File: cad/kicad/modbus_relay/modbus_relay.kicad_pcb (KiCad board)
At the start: 4 copper layers, 75 x 107 mm, 145 parts, among them J10 Conn_02x03_Odd_Even, J11 Screw_Terminal_01x02, J2 Screw_Terminal_01x03, J4 Screw_Terminal_01x02, J5 Screw_Terminal_01x03, J6 Screw_Terminal_01x03, J7 Screw_Terminal_01x03, J8 Screw_Terminal_01x03, J9 Screw_Terminal_01x02, K1 Relay_SPDT, Q1 BSS138, Q2 BSS138, Q3 BSS138, Q4 BSS138, Q6 AO3401A, SW1 SW_Push, U1 LT1785AxS8, U2 ATtiny3227-M, U3 LMR33630ADDA, U4 AMC3330

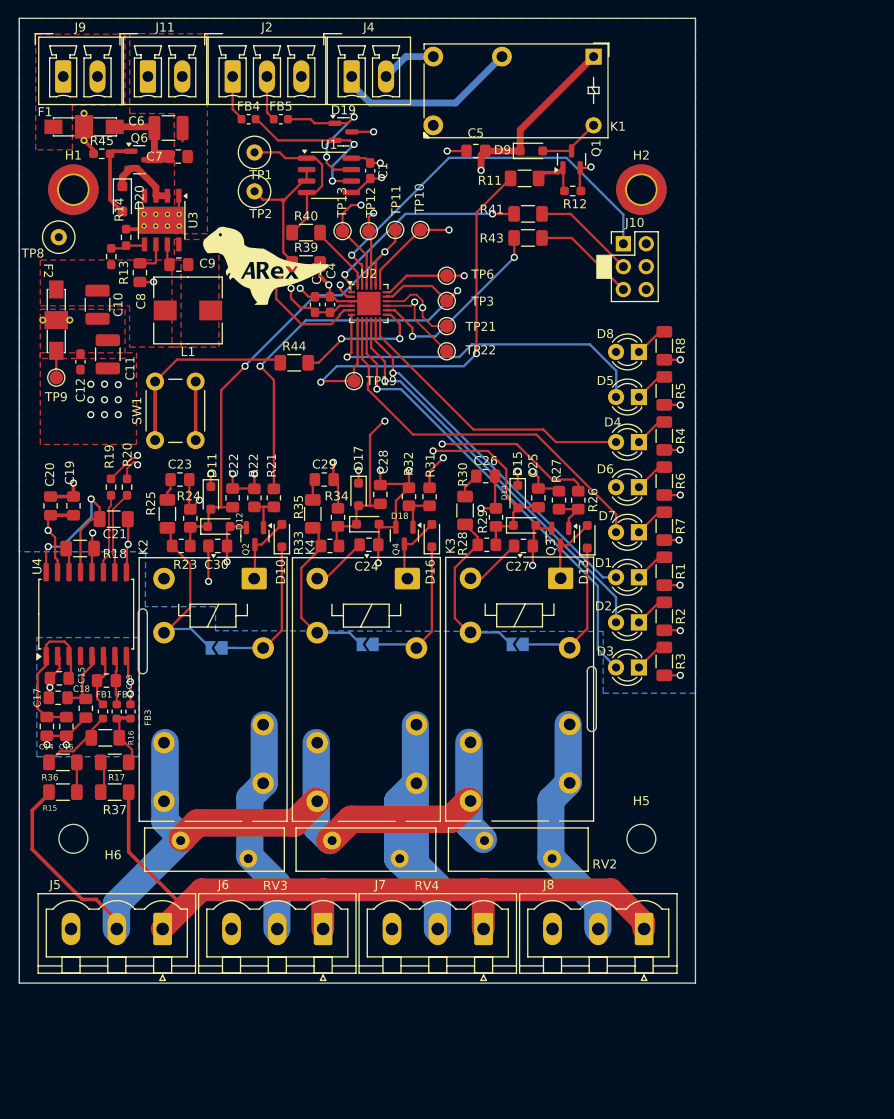
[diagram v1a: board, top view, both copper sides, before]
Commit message: Double sided version
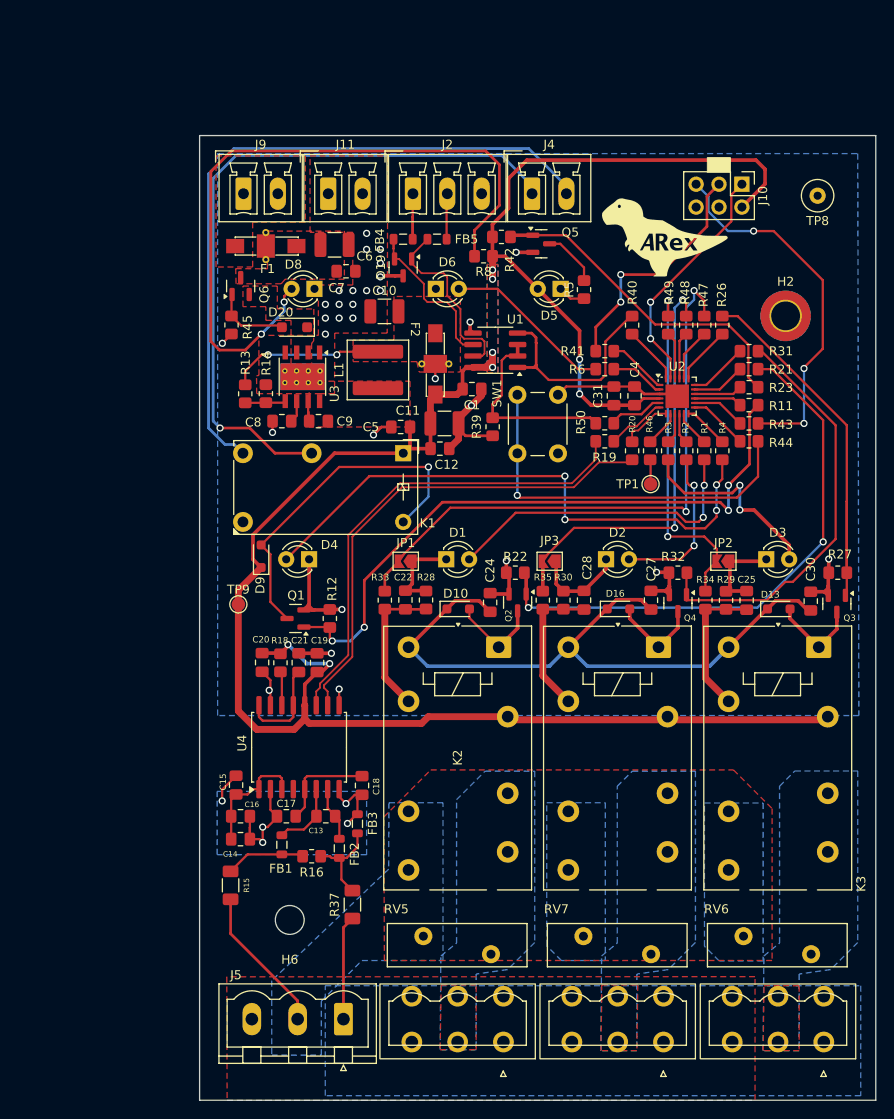
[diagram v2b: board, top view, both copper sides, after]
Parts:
- removed C23, C26, C29: 100n, Capacitor_SMD:C_0805_2012Metric_Pad1.18x1.45mm_HandSolder
- removed D11, D12, D14, D15, D17, D18: BAS16, Diode_SMD:D_SOD-323_HandSoldering
- removed D7: G, LED_THT:LED_D3.0mm
- removed H1: MountingHole_Pad, MountingHole:MountingHole_3.2mm_M3_DIN965_Pad_TopBottom
- removed H5: MountingHole, MountingHole:MountingHole_3.2mm_M3
- removed J6: Screw_Terminal_01x03, Connector_Phoenix_MSTB:PhoenixContact_MSTBVA_2,5_3-G-5,08_1x03_P5.08mm_Vertical
- removed R17, R36: 20K, Resistor_SMD:R_1206_3216Metric_Pad1.30x1.75mm_HandSolder
- removed R24: 1k, Resistor_SMD:R_0805_2012Metric_Pad1.20x1.40mm_HandSolder
- removed R25: 100, Resistor_SMD:R_1206_3216Metric_Pad1.30x1.75mm_HandSolder
- removed R7: 680, Resistor_SMD:R_1206_3216Metric_Pad1.30x1.75mm_HandSolder
- removed RV2, RV3, RV4: 471K, adarwoo:MOV471
- removed TP10, TP11, TP12, TP13, TP19, TP21, TP22, TP3, TP6: TestPoint_Small, TestPoint:TestPoint_Pad_D1.5mm
- removed TP2: TestPoint, TestPoint:TestPoint_Loop_D3.50mm_Drill0.9mm_Beaded
- added J12: 1785955, Phenix contact:CONN_1943548, F.Cu at (156.4, 141.0)
- added Q5: BSS138, Package_TO_SOT_SMD:SOT-23, F.Cu at (147.9, 55.0)
- added R42: 10k, Resistor_SMD:R_0805_2012Metric_Pad1.20x1.40mm_HandSolder, F.Cu at (143.5, 54.2)
- added R46: 332, Resistor_SMD:R_0805_2012Metric_Pad1.20x1.40mm_HandSolder, F.Cu at (160.0, 78.0)
- added R47: 332, Resistor_SMD:R_0805_2012Metric_Pad1.20x1.40mm_HandSolder, F.Cu at (166.0, 64.0)
- added R48: 332, Resistor_SMD:R_0805_2012Metric_Pad1.20x1.40mm_HandSolder, F.Cu at (164.0, 64.0)
- added R49: 332, Resistor_SMD:R_0805_2012Metric_Pad1.20x1.40mm_HandSolder, F.Cu at (162.0, 64.0)
- added R50: 332, Resistor_SMD:R_0805_2012Metric_Pad1.20x1.40mm_HandSolder, F.Cu at (154.9, 74.9)
- added RV5: 471K, adarwoo:MOV471, F.Cu at (138.6, 133.0)
- added RV6: 471K, adarwoo:MOV471, F.Cu at (174.1, 133.0)
- added RV7: 471K, adarwoo:MOV471, F.Cu at (156.4, 133.0)
- C1, C12, C31, C4: footprint Capacitor_SMD:C_0603_1608Metric_Pad1.08x0.95mm_HandSolder -> Capacitor_SMD:C_0805_2012Metric_Pad1.18x1.45mm_HandSolder
- C21: footprint Capacitor_SMD:C_1206_3216Metric_Pad1.33x1.80mm_HandSolder -> Capacitor_SMD:C_0805_2012Metric_Pad1.18x1.45mm_HandSolder
- D20: value BZT52B51 -> BZT52B12
- FB1, FB2, FB3, FB4, FB5: footprint Inductor_SMD:L_0603_1608Metric -> Inductor_SMD:L_0805_2012Metric
- J7, J8: value Screw_Terminal_01x03 -> 1785955; footprint Connector_Phoenix_MSTB:PhoenixContact_MSTBVA_2,5_3-G-5,08_1x03_P5.08mm_Vertical -> Phenix contact:CONN_1943548
- JP1, JP2, JP3: moved to F.Cu
- L1: value 15uH -> 10uH; footprint Inductor_SMD:L_Wuerth_HCM-7070 -> Inductor_SMD:L_Bourns_SRP6060FA
- R1, R11, R16, R18, R2, R3, R39, R4, R40, R41, R43, R44, R5, R6, R8: footprint Resistor_SMD:R_1206_3216Metric_Pad1.30x1.75mm_HandSolder -> Resistor_SMD:R_0805_2012Metric_Pad1.20x1.40mm_HandSolder
- R12, R13, R14, R19, R20: footprint Resistor_SMD:R_0603_1608Metric_Pad0.98x0.95mm_HandSolder -> Resistor_SMD:R_0805_2012Metric_Pad1.20x1.40mm_HandSolder
- R23: value 3k83 -> 22
- R28, R33: value 3k83 -> 332
- R29, R34: value 1k -> 332
- R30, R35: value 100 -> 332; footprint Resistor_SMD:R_1206_3216Metric_Pad1.30x1.75mm_HandSolder -> Resistor_SMD:R_0805_2012Metric_Pad1.20x1.40mm_HandSolder
- R45: value 22 -> 10K; footprint Resistor_SMD:R_0603_1608Metric_Pad0.98x0.95mm_HandSolder -> Resistor_SMD:R_0805_2012Metric_Pad1.20x1.40mm_HandSolder
- TP1: value TestPoint -> TestPoint_Probe; footprint TestPoint:TestPoint_Loop_D3.50mm_Drill0.9mm_Beaded -> TestPoint:TestPoint_Pad_D1.5mm
- moved TP8 84.3 mm to (178.5, 49.7)
- moved C30 66.1 mm to (177.8, 94.6), turned to 90 degrees
- moved R23 65.4 mm to (170.9, 70.9)
- moved Q1 59.4 mm to (120.6, 96.6), turned to 180 degrees
- moved TP1 57.3 mm to (160.0, 81.7)
- moved R20 56.2 mm to (158.0, 78.0)
- moved R19 55.0 mm to (154.9, 76.9), turned to 0 degrees
- moved R21 54.6 mm to (170.9, 68.9), turned to 0 degrees
- moved R12 54.5 mm to (124.4, 96.6), turned to 90 degrees
- moved D9 54.0 mm to (116.8, 89.7), turned to 90 degrees
- moved R44 51.2 mm to (170.9, 76.9), turned to 180 degrees
- moved K1 48.8 mm to (132.6, 78.2)
- moved G*** 44.4 mm to (161.6, 54.3)
- moved F2 42.3 mm to (136.1, 68.3)
- moved R34 41.8 mm to (166.1, 94.5), turned to -90 degrees
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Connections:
- net Net-(D19-A1) renamed /FILT+
- net Net-(D19-A2) renamed /FILT-
- C22 pad 1: RELAY_CHECK_1 -> Net-(C22-Pad1)
- C24 pad 1: +24V -> V_IN
- C25 pad 1: RELAY_CHECK_3 -> Net-(C25-Pad1)
- C27 pad 1: +24V -> V_IN
- C28 pad 1: RELAY_CHECK_2 -> Net-(C28-Pad1)
- C30 pad 1: +24V -> V_IN
- D1 pad 1: Net-(D1-K) -> GND
- D1 pad 2: LED_RELAY_1 -> Net-(D1-A)
- D10 pad 1: +24V -> V_IN
- D13 pad 1: +24V -> V_IN
- D16 pad 1: +24V -> V_IN
- D2 pad 1: Net-(D2-K) -> GND
- D2 pad 2: LED_RELAY_2 -> Net-(D2-A)
- D3 pad 1: Net-(D3-K) -> GND
- D3 pad 2: LED_RELAY_3 -> Net-(D3-A)
- D4 pad 1: Net-(D4-K) -> GND
- D4 pad 2: LED_MAINS -> Net-(D4-A)
- D5 pad 2: LED_FAULT -> VCC
- D6 pad 1: Net-(D6-K) -> GND
- D6 pad 2: LED_RX -> Net-(D6-A)
- D8 pad 1: Net-(D8-K) -> GND
- D8 pad 2: VCC -> Net-(D8-A)
- J7 pad 2: RELAY_OUT_2 -> MAINS_N
- J7 pad 3: Earth -> RELAY_OUT_1
- J8 pad 2: RELAY_OUT_3 -> MAINS_N
- J8 pad 3: Earth -> RELAY_OUT_3
- JP1 pad 1: +24V -> GND
- JP1 pad 2: Net-(JP1-B) -> RELAY_CHECK_1
- JP2 pad 1: +24V -> GND
- JP2 pad 2: Net-(JP2-B) -> RELAY_CHECK_3
- JP3 pad 1: +24V -> GND
- JP3 pad 2: Net-(JP3-B) -> RELAY_CHECK_2
- K2 pad 11: Net-(JP1-B) -> Net-(C22-Pad1)
- K2 pad 12: +24V -> VCC
- K2 pad A1: +24V -> V_IN
- K3 pad 11: Net-(JP2-B) -> Net-(C25-Pad1)
- K3 pad 12: +24V -> VCC
- K3 pad A1: +24V -> V_IN
- K4 pad 11: Net-(JP3-B) -> Net-(C28-Pad1)
- K4 pad 12: +24V -> VCC
- K4 pad A1: +24V -> V_IN
- R1 pad 1: Net-(D1-K) -> LED_RELAY_1
- R1 pad 2: GND -> Net-(D1-A)
- R11 pad 1: ES_CMD -> ~{ESTOP}
- R15 pad 2: Net-(R15-Pad2) -> Net-(FB1-Pad1)
- R2 pad 1: Net-(D2-K) -> LED_RELAY_2
- R2 pad 2: GND -> Net-(D2-A)
- R23 pad 1: Net-(JP1-B) -> ~{LED_FAULT}
- R23 pad 2: RELAY_CHECK_1 -> Net-(Q5-G)
- R28 pad 1: Net-(JP2-B) -> Net-(C22-Pad1)
- R28 pad 2: RELAY_CHECK_3 -> GND
- R29 pad 1: RELAY_CHECK_3 -> Net-(C25-Pad1)
- R3 pad 1: Net-(D3-K) -> LED_RELAY_3
- R3 pad 2: GND -> Net-(D3-A)
- R30 pad 1: Net-(JP2-B) -> Net-(C28-Pad1)
- R30 pad 2: Net-(C26-Pad1) -> GND
- R33 pad 1: Net-(JP3-B) -> RELAY_CHECK_1
- R33 pad 2: RELAY_CHECK_2 -> Net-(C22-Pad1)
- R34 pad 1: RELAY_CHECK_2 -> RELAY_CHECK_3
- R34 pad 2: GND -> Net-(C25-Pad1)
- R35 pad 1: Net-(JP3-B) -> RELAY_CHECK_2
- R35 pad 2: Net-(C29-Pad1) -> Net-(C28-Pad1)
- R37 pad 1: Net-(R17-Pad2) -> Net-(FB2-Pad1)
- R4 pad 1: Net-(D4-K) -> LED_MAINS
- R4 pad 2: GND -> Net-(D4-A)
- R5 pad 2: GND -> Net-(Q5-D)
- R6 pad 1: Net-(D6-K) -> LED_RX
- R6 pad 2: GND -> Net-(D6-A)
- R8 pad 1: Net-(D8-K) -> VCC
- R8 pad 2: GND -> Net-(D8-A)
- TP1 pad 1: Net-(U1-DI) -> Net-(R46-Pad1)
- U2 pad 15: ISO_IN+ -> ~{ESTOP}
- U2 pad 16: ISO_IN- -> ~{LED_FAULT}
- U2 pad 20: RELAY_CHECK_1 -> Net-(U2-PC3)
- U2 pad 21: RELAY_CHECK_2 -> Net-(U2-PC4)
- U2 pad 22: RELAY_CHECK_3 -> Net-(U2-PC5)
- U2 pad 5: Net-(U1-DE) -> Net-(U2-PA4)
- U2 pad 6: LED_FAULT -> ISO_IN+
- U2 pad 7: ES_CMD -> ISO_IN-
- U2 pad 8: LED_TX -> Net-(U2-PA7)
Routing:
- net VCC: track 48.7 -> 230.5 mm, vias 17 -> 8
- net MAINS_L: track 101.9 -> 16.4 mm
- net Net-(D8-A): track 0.00 -> 76.9 mm, vias 0 -> 2
- net V_IN: track 0.00 -> 75.8 mm
- net ES_2: track 6.33 -> 76.6 mm
- net MAINS_N: track 81.5 -> 11.9 mm
- net +24V: track 67.0 -> 0.00 mm, vias 1 -> 0
- net Net-(Q1-G): track 5.83 -> 71.3 mm, vias 0 -> 4
- net Net-(D4-A): track 0.00 -> 64.0 mm, vias 0 -> 4
- net Net-(Q2-G): track 4.79 -> 62.8 mm, vias 0 -> 2
- net ES_1: track 20.5 -> 78.0 mm, vias 0 -> 1
- net ES_CMD: track 50.2 -> 0.00 mm, vias 2 -> 0
- net LED_RELAY_3: track 51.5 -> 3.43 mm, vias 1 -> 0
- net RELAY_CMD_3: track 53.0 -> 6.50 mm, vias 2 -> 0
- net ISO_IN+: track 52.6 -> 6.65 mm, vias 2 -> 0
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- added copper zone on F.Cu, net /Power supply/VIN
- added copper zone on F.Cu, net Earth
- added copper zone on B.Cu, net MAINS_L
- added copper zone on F.Cu, net MAINS_L
- added copper zone on B.Cu, net MAINS_N
- added copper zone on F.Cu, net Net-(Q6-D)
- added copper zone on B.Cu, net RELAY_OUT_1
- added copper zone on F.Cu, net RELAY_OUT_1
- added copper zone on B.Cu, net RELAY_OUT_2
- added copper zone on F.Cu, net RELAY_OUT_2
- added copper zone on B.Cu, net RELAY_OUT_3
- added copper zone on F.Cu, net RELAY_OUT_3
- added copper zone on B.Cu, net VCC
- removed copper zone on In1.Cu, net +24V
- removed copper zone on In1.Cu, net Earth
- removed copper zone on In2.Cu, net Earth
- removed copper zone on In2.Cu, net GND
- removed copper zone on In2.Cu, net GNDPWR
- removed copper zone on In1.Cu, net VCC
- removed copper zone on In2.Cu, net VCC
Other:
- outline, holes or cut-outs redrawn
- copper layers 4 -> 2

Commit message: Double sided version
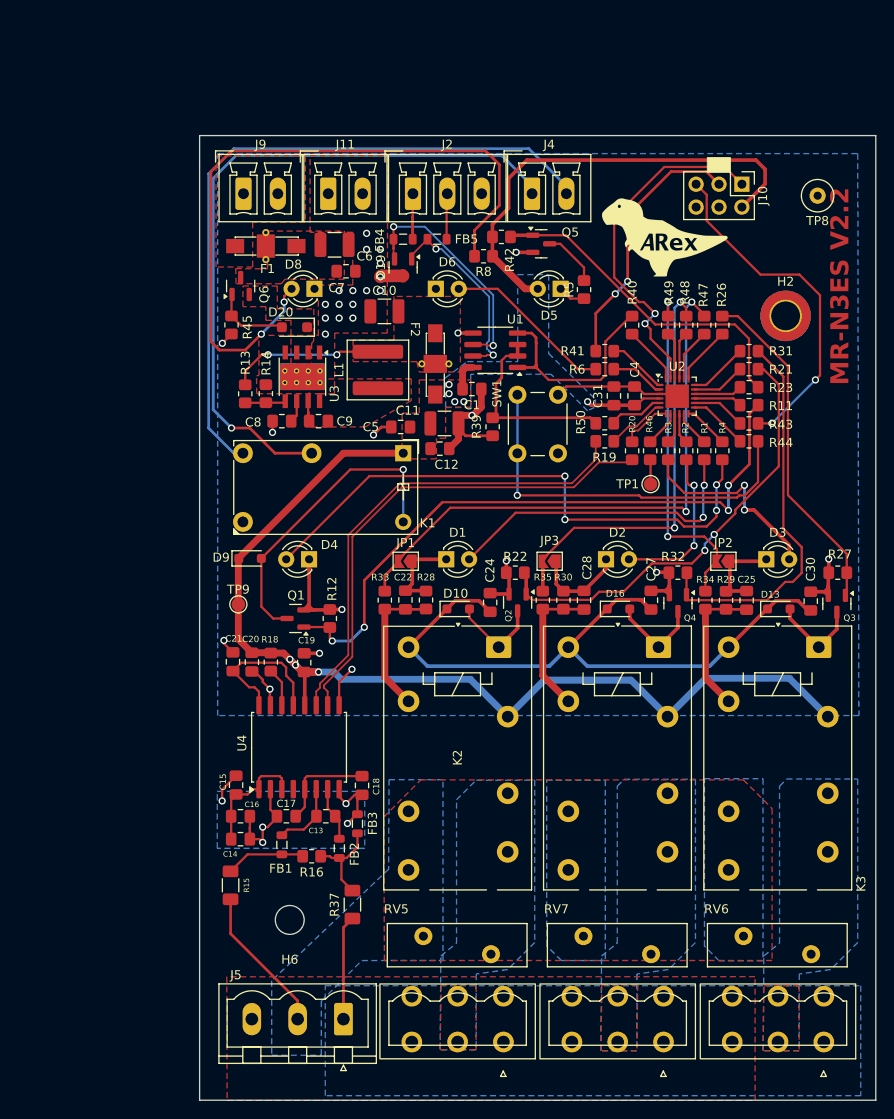
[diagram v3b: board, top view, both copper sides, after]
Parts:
- moved C21 7.30 mm to (113.7, 101.4)
- moved C19 1.43 mm to (121.6, 101.5)
- moved D9 1.25 mm to (115.6, 89.9), turned to 0 degrees
- moved C20 1.14 mm to (115.8, 101.4)
- moved R18 1.07 mm to (117.9, 101.4)
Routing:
- net VCC: track 230.5 -> 179.5 mm
- net Net-(Q2-G): track 62.8 -> 49.6 mm
- net Net-(J10-Pin_1): track 26.7 -> 39.0 mm
- net /FILT-: track 18.6 -> 26.7 mm, vias 0 -> 2
- net Net-(Q3-G): track 45.7 -> 37.8 mm
- net Net-(U4-DCDC_IN): track 10.7 -> 16.4 mm
- net Net-(D9-A): track 38.7 -> 34.4 mm
- net Net-(Q4-G): track 47.1 -> 43.7 mm
- net Net-(J10-Pin_5): track 41.3 -> 38.5 mm, vias 3 -> 2
- net Net-(J10-Pin_3): track 26.6 -> 29.3 mm
- net RELAY_CHECK_1: track 66.8 -> 64.2 mm
- net GND: track 113.5 -> 115.4 mm
- net /FILT+: track 20.7 -> 21.6 mm, vias 0 -> 2
- net ES_1: track 78.0 -> 77.3 mm
- net RELAY_CHECK_2: track 47.2 -> 46.7 mm
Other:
- board text added: "MR-N3ES V2.2"

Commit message: New PCBs fixed and tested. Clean defs
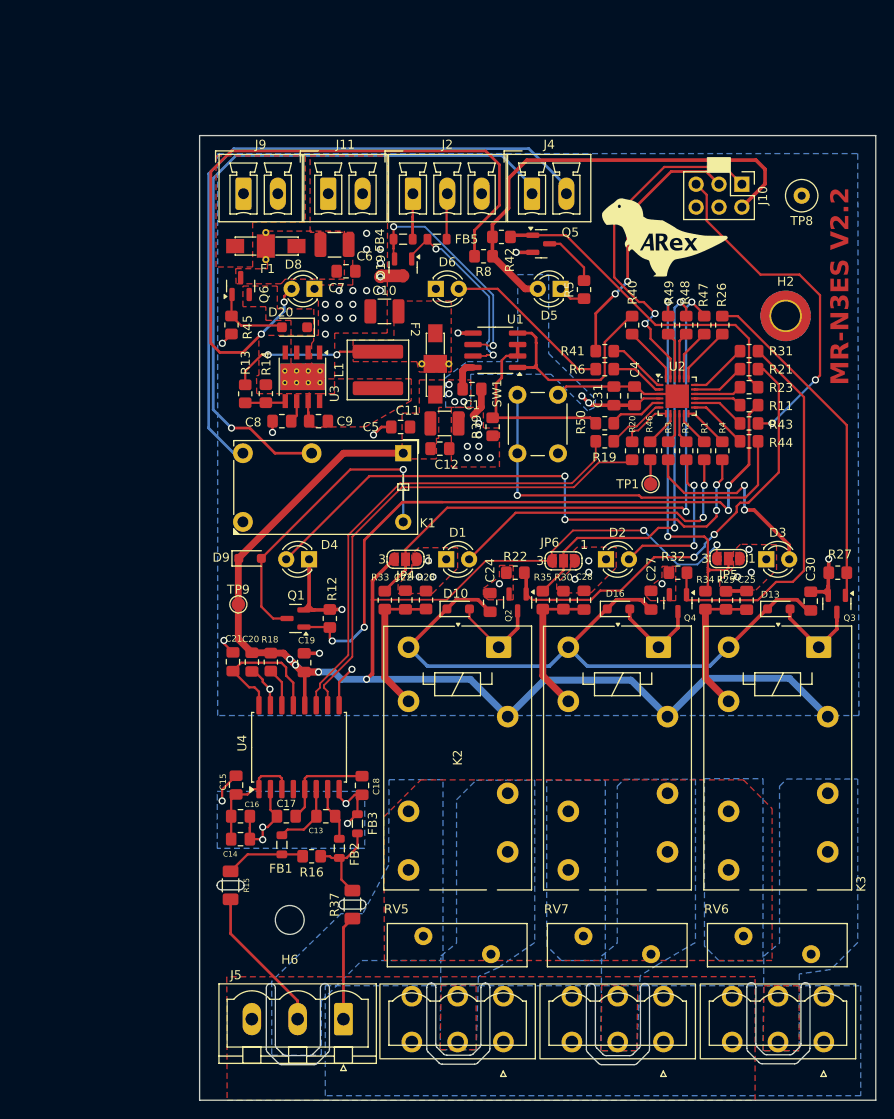
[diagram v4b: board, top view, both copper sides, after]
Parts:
- removed JP1, JP2, JP3: SolderJumper_2_Open, Jumper:SolderJumper-2_P1.3mm_Open_TrianglePad1.0x1.5mm
- added JP4: SolderJumper_3_Open, Jumper:SolderJumper-3_P1.3mm_Open_RoundedPad1.0x1.5mm_NumberLabels, F.Cu at (132.8, 90.0)
- added JP5: SolderJumper_3_Open, Jumper:SolderJumper-3_P1.3mm_Open_RoundedPad1.0x1.5mm_NumberLabels, F.Cu at (168.7, 89.9)
- added JP6: SolderJumper_3_Open, Jumper:SolderJumper-3_P1.3mm_Open_RoundedPad1.0x1.5mm_NumberLabels, F.Cu at (150.4, 90.2)
- moved TP8 1.76 mm to (176.8, 49.7)
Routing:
- net VCC: track 179.5 -> 241.1 mm, vias 8 -> 12
- net GND: track 115.4 -> 68.8 mm, vias 30 -> 45
- net RELAY_CHECK_3: track 38.8 -> 42.1 mm
- net Net-(Q1-G): track 71.3 -> 73.9 mm
- net RELAY_CHECK_2: track 46.7 -> 45.9 mm
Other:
- outline, holes or cut-outs redrawn

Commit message: Fixed the V_IN VIN label issue
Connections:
- net V_IN renamed VIN
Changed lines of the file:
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@@
 	(net 87 "/FILT+")
 	(net 88 "/FILT-")
-	(net 89 "V_IN")
+	(net 89 "VIN")
 	(net 90 "unconnected-(K1-Pad12)")
 	(footprint "TestPoint:TestPoint_Pad_D1.5mm"
@@
 			(layers "F.Cu" "F.Mask" "F.Paste")
 			(roundrect_rratio 0.212766)
-			(net 89 "V_IN")
+			(net 89 "VIN")
 			(pintype "passive")
 		)
@@
 			(layers "F.Cu" "F.Mask" "F.Paste")
 			(roundrect_rratio 0.25)
-			(net 89 "V_IN")
+			(net 89 "VIN")
 			(pinfunction "K")
 			(pintype "passive")
@@
 			(layers "*.Cu" "*.Mask")
 			(remove_unused_layers no)
-			(net 89 "V_IN")
+			(net 89 "VIN")
 			(pintype "passive")
 		)
@@
 			(layers "*.Cu" "*.Mask")
 			(remove_unused_layers no)
-			(net 89 "V_IN")
+			(net 89 "VIN")
 			(pintype "passive")
 		)
@@
 			(layers "F.Cu" "F.Mask" "F.Paste")
 			(roundrect_rratio 0.212766)
-			(net 89 "V_IN")
+			(net 89 "VIN")
 			(pintype "passive")
 		)
@@
 			(layers "*.Cu" "*.Mask")
 			(remove_unused_layers no)
-			(net 89 "V_IN")
+			(net 89 "VIN")
 			(pintype "passive")
 		)
@@
 			(layers "F.Cu" "F.Mask" "F.Paste")
 			(roundrect_rratio 0.212766)
-			(net 89 "V_IN")
+			(net 89 "VIN")
 			(pintype "passive")
 		)
@@
 			(layers "F.Cu" "F.Mask" "F.Paste")
 			(roundrect_rratio 0.25)
-			(net 89 "V_IN")
+			(net 89 "VIN")
 			(pinfunction "K")
 			(pintype "passive")
@@
 			(layers "F.Cu" "F.Mask" "F.Paste")
 			(roundrect_rratio 0.25)
-			(net 89 "V_IN")
+			(net 89 "VIN")
 			(pinfunction "K")
 			(pintype "passive")
